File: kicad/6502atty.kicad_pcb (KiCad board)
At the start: 2 copper layers, 106.4 x 115.6 mm, 103 parts, among them J1 Conn_01x04_Pin, J10 Conn_01x04_Pin, J11 Conn_01x03_Pin, J12 Conn_01x02_Pin, J2 Conn_01x02_Pin, J3 Conn_02x03_Odd_Even, J4 Conn_01x03_Pin, J5 Conn_01x06_Pin, J6 Conn_01x04_Pin, J7 Conn_01x10_Pin, J8 Conn_01x03_Pin, J9 Conn_01x10_Pin, SW1 SW_Push, U1 ATmega164P-20P, U10 74LS08, U11 74LS138, U12 74LS574, U2 74LS112, U3 W65C02SxP, U4 74LS574, U5 74HC245, U6 27C128, U7 KM62256CLP, U8 74LS00, U9 74LS00, Y1 18.432MHz

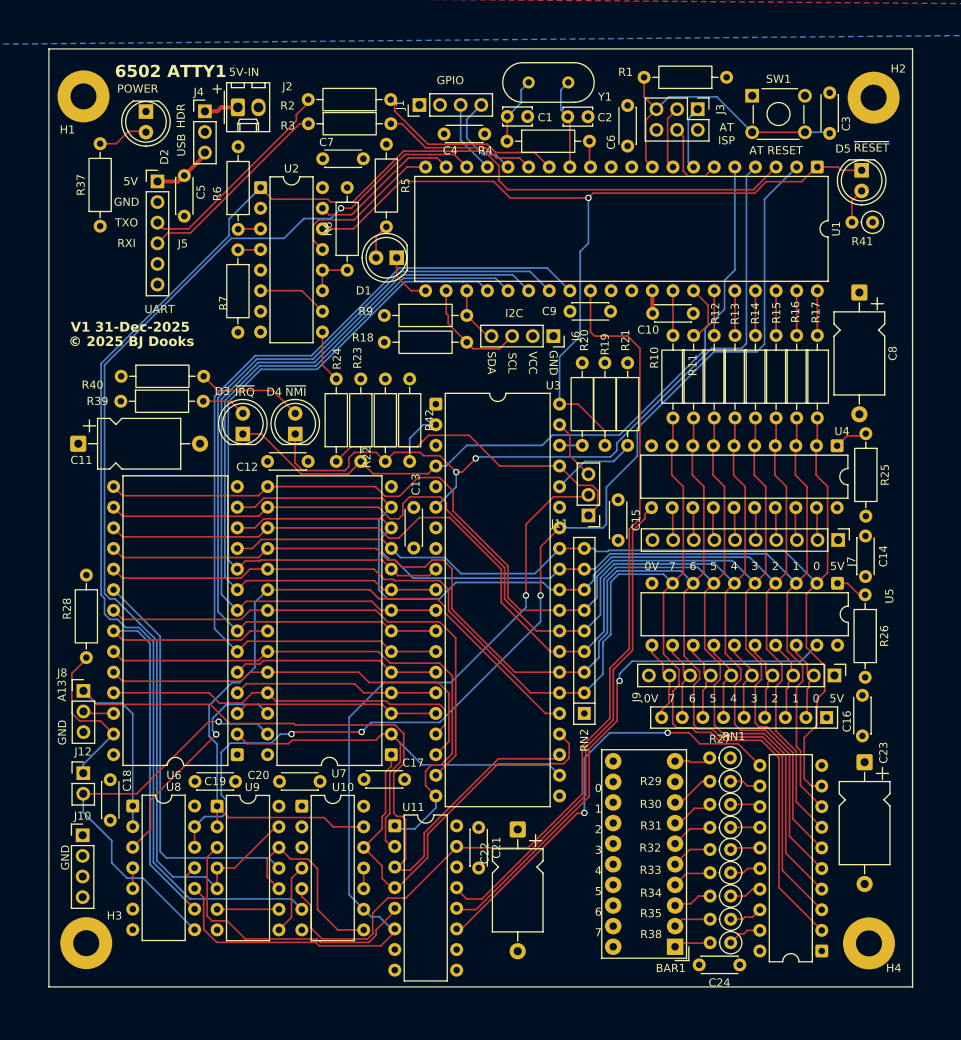
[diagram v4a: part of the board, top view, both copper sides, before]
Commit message: pcb updates, remove resistor on xtal, smaller board
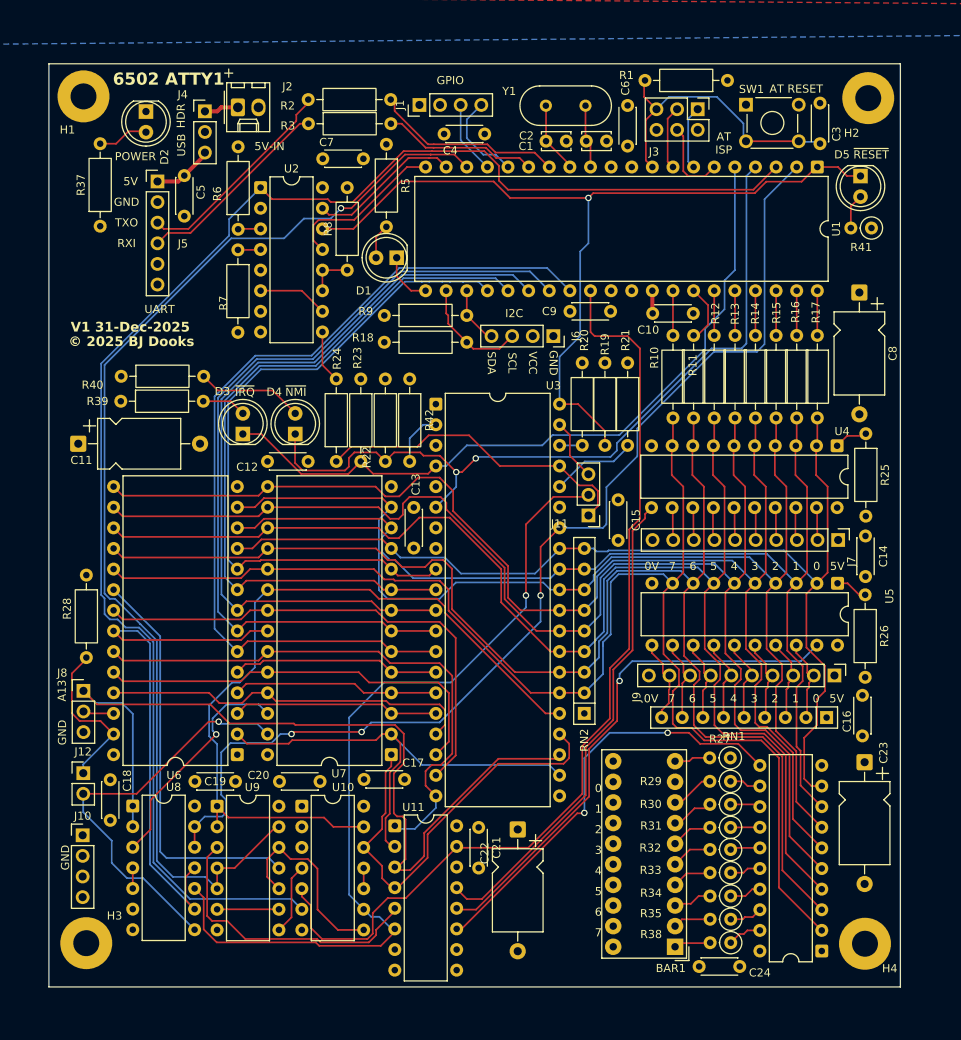
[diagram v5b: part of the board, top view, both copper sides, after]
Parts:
- removed R4: 1K, Resistor_THT:R_Axial_DIN0207_L6.3mm_D2.5mm_P10.16mm_Horizontal
- moved C1 10.2 mm to (78.2, 23.1)
- moved Y1 7.56 mm to (78.1, 18.7), turned to 180 degrees
- moved C2 4.03 mm to (73.2, 23.1)
- moved C3 1.74 mm to (107.0, 23.4)
- moved SW1 1.34 mm to (97.8, 18.6)
- moved D5 0.72 mm to (111.9, 27.4)
- moved R41 0.72 mm to (113.3, 33.8)
- moved H2 0.67 mm to (112.9, 17.8)
- moved H4 0.49 mm to (112.5, 122.0)
- moved R1 0.40 mm to (95.6, 15.6)
- moved C24 0.20 mm to (97.1, 124.8)
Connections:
- net Net-(U1-XTAL1) renamed /Atmel Controller/AT_XTI
- C1 pad 1: Net-(C1-Pad1) -> /Atmel Controller/AT_XTO
- U1 pad 12: Net-(U1-XTAL2) -> /Atmel Controller/AT_XTO
- Y1 pad 1: Net-(C1-Pad1) -> /Atmel Controller/AT_XTO
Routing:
- net Net-(C1-Pad1): track 8.34 -> 0.00 mm
- net /Atmel Controller/AT_XTO: track 0.00 -> 7.99 mm
- net Net-(U1-XTAL2): track 3.23 -> 0.00 mm
- net /Atmel Controller/AT_XTI: track 11.3 -> 8.78 mm
- net Net-(BAR1J-A): track 4.94 -> 4.43 mm
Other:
- board size 106.4 x 115.6 mm -> 104.9 x 113.7 mm

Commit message: pcb: move closer to 0,0 origin, fixup routing on serial
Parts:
- R1: footprint Resistor_THT:R_Axial_DIN0207_L6.3mm_D2.5mm_P10.16mm_Horizontal -> Resistor_THT:R_Axial_DIN0207_L6.3mm_D2.5mm_P2.54mm_Vertical
- moved BAR1 18.3 mm to (77.1, 108.5)
- moved C13 18.3 mm to (44.9, 59.4)
- moved C19 18.3 mm to (18.0, 88.1)
- moved C20 18.3 mm to (28.4, 88.1)
- moved C23 18.3 mm to (100.5, 85.8)
- moved C9 18.3 mm to (69.2, 30.2)
- moved J10 18.3 mm to (4.15, 94.8)
- moved J12 18.3 mm to (4.22, 87.1)
- moved J7 18.3 mm to (97.2, 58.4)
- moved J9 18.3 mm to (96.8, 75.1)
- moved R10 18.3 mm to (76.9, 33.2)
- moved R12 18.3 mm to (81.9, 33.2)
- moved R13 18.3 mm to (84.5, 33.2)
- moved R14 18.3 mm to (87.0, 33.2)
- moved R16 18.3 mm to (92.1, 33.2)
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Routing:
- net /Atmel Controller/U_5V: track 7.49 -> 18.5 mm
- net /Atmel Controller/U_RXI: track 24.7 -> 30.5 mm
- net /Atmel Controller/~{AT_RESET}: track 36.9 -> 35.2 mm
- net (no net): track 0.00 -> 0.68 mm
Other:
- board size 104.9 x 113.7 mm -> 104.9 x 113.3 mm
- board text added: "6052"
- board text added: "ATMEGA"
- board text added: "RAM"
- board text added: "ROM/RAM"
